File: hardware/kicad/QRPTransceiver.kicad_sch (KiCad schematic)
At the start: 0 parts

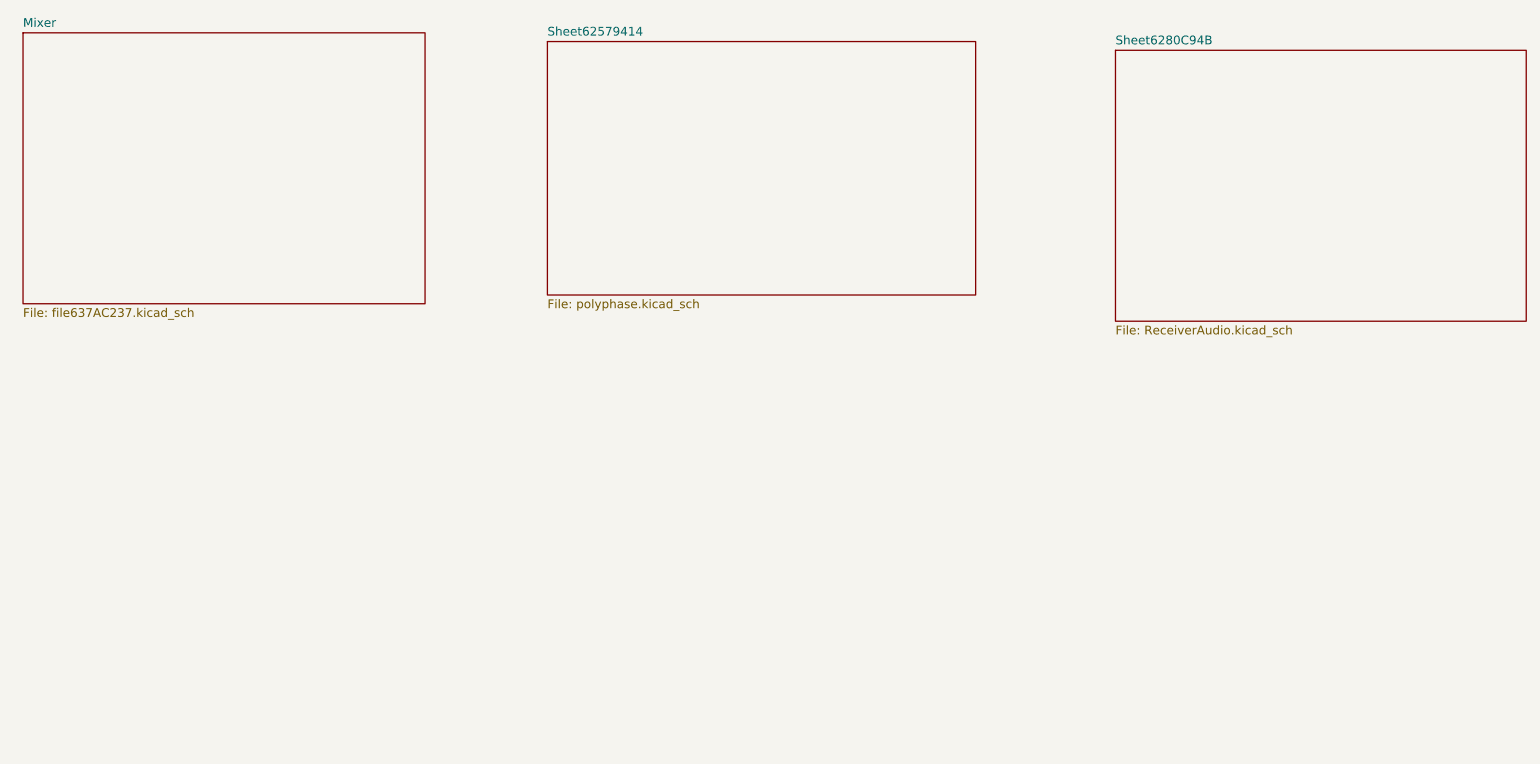
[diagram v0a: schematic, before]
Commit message: Fixed quadrature generation PCB excirt circuit in draft
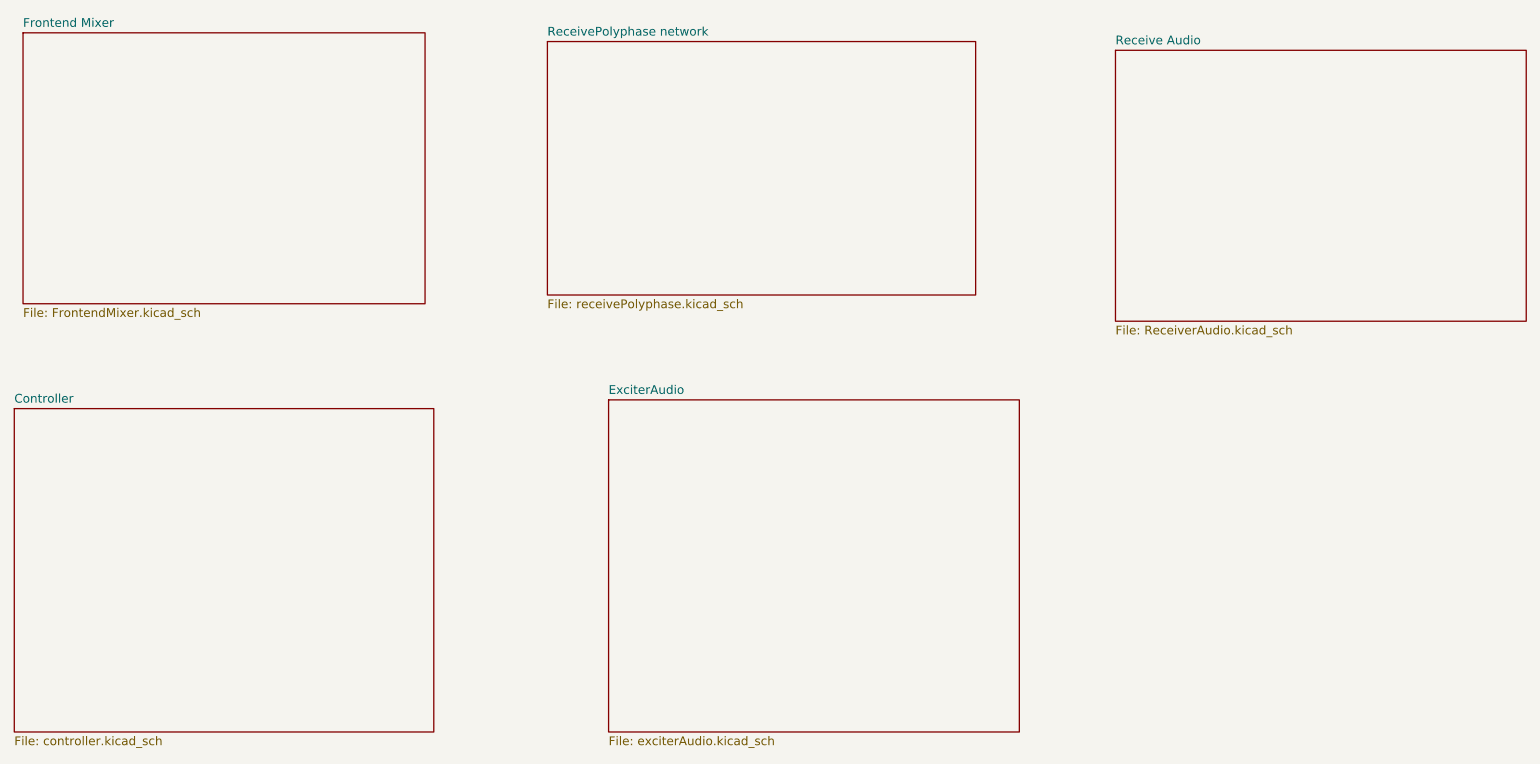
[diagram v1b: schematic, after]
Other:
- sheet Mixer renamed Frontend Mixer
- sheet Sheet62579414 renamed ReceivePolyphase network
- sheet Sheet6280C94B renamed Receive Audio
- added sheet Controller (controller.kicad_sch)
- added sheet ExciterAudio (exciterAudio.kicad_sch)
- sheet Frontend Mixer: file file637AC237.kicad_sch -> FrontendMixer.kicad_sch
- sheet ReceivePolyphase network: file polyphase.kicad_sch -> receivePolyphase.kicad_sch
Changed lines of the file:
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@@
 			(color 0 0 0 0.0000)
 		)
-		(property "Sheetname" "Sheet62579414"
+		(property "Sheetname" "ReceivePolyphase network"
 			(at 102.87 27.2284 0)
 			(effects
@@
 			)
 		)
-		(property "Sheetfile" "polyphase.kicad_sch"
+		(property "Sheetfile" "receivePolyphase.kicad_sch"
 			(at 102.87 65.3546 0)
 			(effects
@@
 			(color 0 0 0 0.0000)
 		)
-		(property "Sheetname" "Sheet6280C94B"
+		(property "Sheetname" "Receive Audio"
 			(at 185.42 28.4984 0)
 			(effects
@@
 			(color 0 0 0 0.0000)
 		)
-		(property "Sheetname" "Mixer"
+		(property "Sheetname" "Frontend Mixer"
 			(at 26.67 25.9584 0)
 			(effects
@@
 			)
 		)
-		(property "Sheetfile" "file637AC237.kicad_sch"
+		(property "Sheetfile" "FrontendMixer.kicad_sch"
 			(at 26.67 66.6246 0)
 			(effects
@@
 				)
 			)
+		)
+	)
+	(sheet
+		(at 25.4 81.28)
+		(size 60.96 46.99)
+		(fields_autoplaced yes)
+		(stroke
+			(width 0.1524)
+			(type solid)
+		)
+		(fill
+			(color 0 0 0 0.0000)
+		)
+		(property "Sheetname" "Controller"
+			(at 25.4 80.5684 0)
+			(effects
+				(font
+					(size 1.27 1.27)
+				)
+				(justify left bottom)
+			)
+		)
+		(property "Sheetfile" "controller.kicad_sch"
+			(at 25.4 128.8546 0)
+			(effects
+				(font
+					(size 1.27 1.27)
+				)
+				(justify left top)
+			)
+		)
+		(instances
+			(project "QRPTransceiver"
+				(path "/2b42efc4-5f47-4ec1-a444-f7c37de69fbf"
+					(page "5")
+				)
+			)
+		)
+	)
+	(sheet
+		(at 111.76 80.01)
+		(size 59.69 48.26)
+		(fields_autoplaced yes)
+		(stroke
+			(width 0.1524)
+			(type solid)
+		)
+		(fill
+			(color 0 0 0 0.0000)
+		)
+		(property "Sheetname" "ExciterAudio"
+			(at 111.76 79.2984 0)
+			(effects
+				(font
+					(size 1.27 1.27)
+				)
+				(justify left bottom)
+			)
+		)
+		(property "Sheetfile" "exciterAudio.kicad_sch"
+			(at 111.76 128.8546 0)
+			(effects
+				(font
+					(size 1.27 1.27)
+				)
+				(justify left top)
+			)
+		)
+		(instances
+			(project "QRPTransceiver"
+				(path "/2b42efc4-5f47-4ec1-a444-f7c37de69fbf"
+					(page "6")
+				)
+			)
